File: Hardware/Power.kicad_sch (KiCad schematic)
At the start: 48 parts, among them U1 LT1963AEST-3.3#TRPBF, U2 TPS5405DR, U3 TPS2115ADRBR, U4 LT1963AEST-3.3#TRPBF

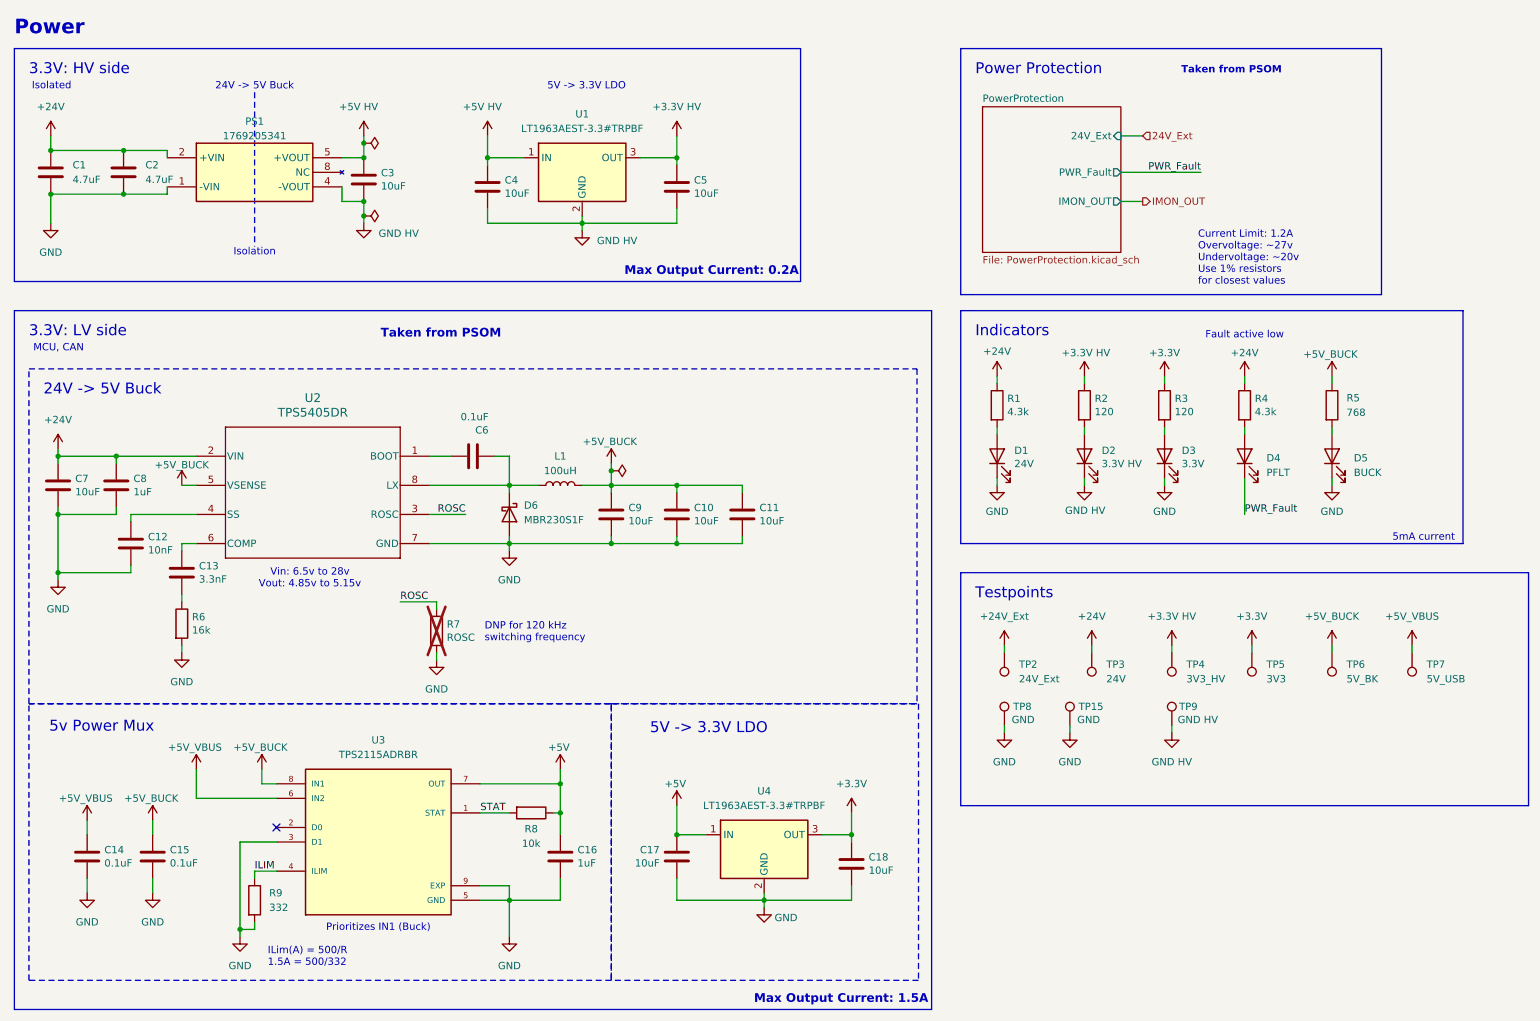
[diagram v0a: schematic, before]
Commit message: RevB Changes (#4)
* added documentation for current range; added VBUS led

* INA common-mode fixed (i think)

* differential amp for LPF

* diff amp / LPF

* some comments so I don't forget what I'm doing

* new TLV symbol, SPDT switch for scrut

* fixed LPF cutoff

* refactored and added LPF docs; added fuse, boot_gpio from USB-UART chip

* i lowk haven't started layout

* slightly cooked

* started layout not really but kind of

* layout stuff

* post review council sch changes: shielded connectors, removed SHDN resistor, diode OR for boot, standardized resistors

* starting routing i think

* almost done with routing

* wow

* drc is happy

* ye

* again

* addressed some comments

* added lcsc part numbers

* generated production files and docs

* updated STEP file

* symbol library

* addressed comments; generated production files, docs

* added Mouser BOM, deleted embedded step files
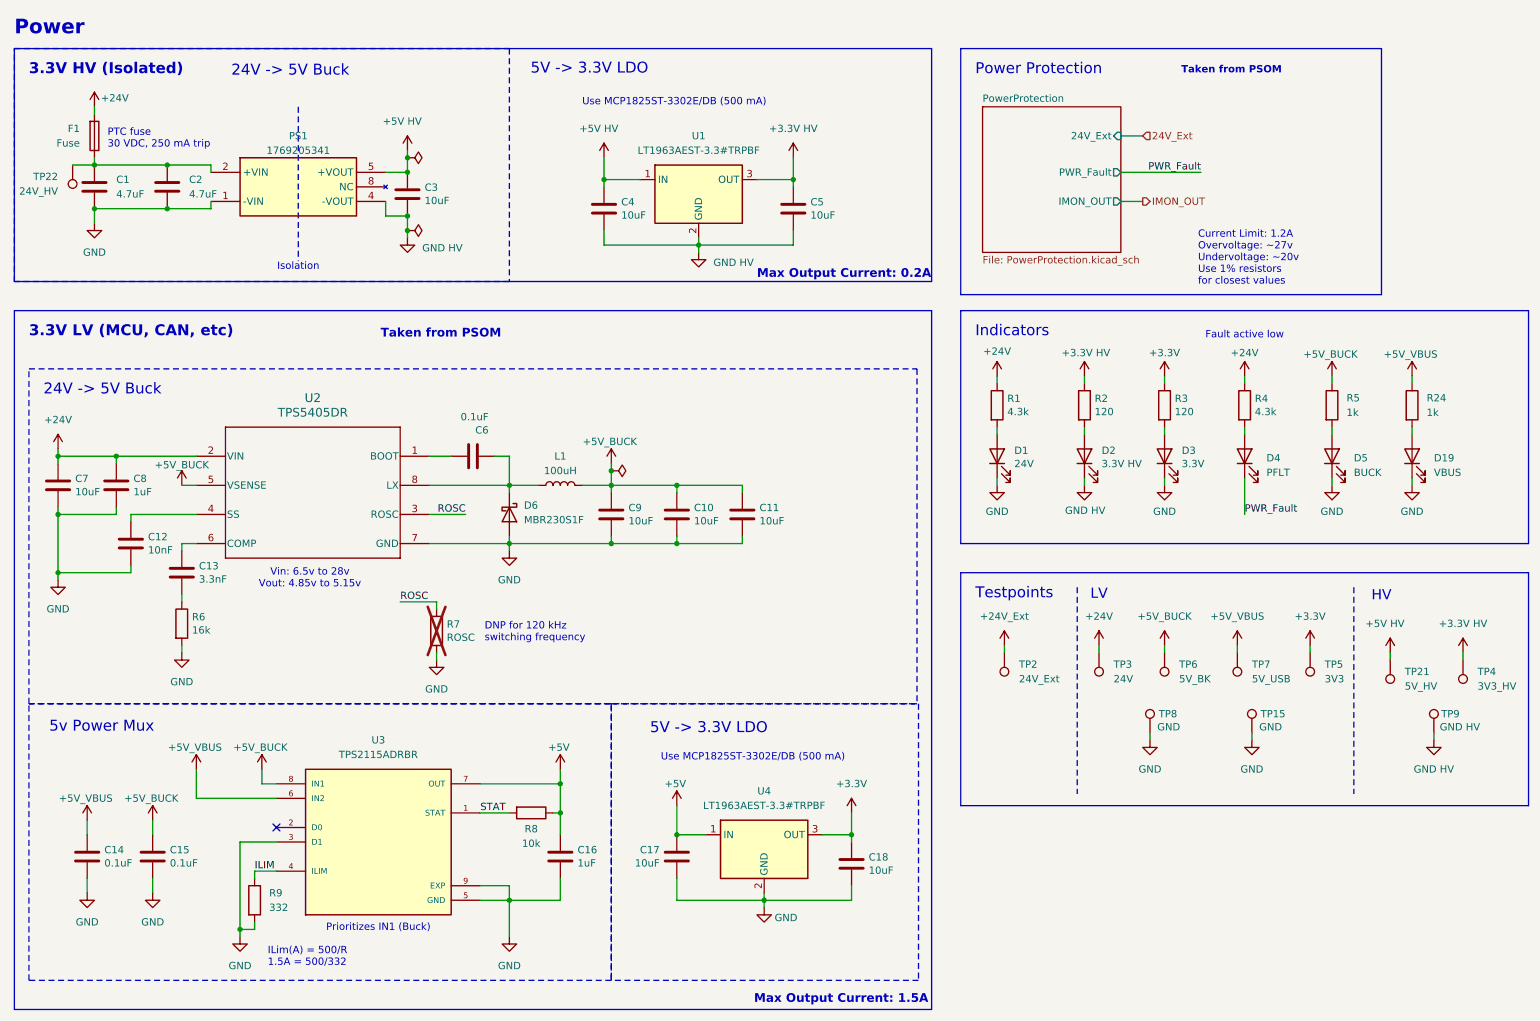
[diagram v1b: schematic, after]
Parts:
- added D19: VBUS, LED_SMD:LED_0603_1608Metric_Pad1.05x0.95mm_HandSolder, symbol Device:LED
- added F1: Fuse, Parts:FUSC3216X125N, symbol Device:Fuse
- added R24: 1k, Resistor_SMD:R_0603_1608Metric_Pad0.98x0.95mm_HandSolder, symbol Device:R
- added TP21: 5V_HV, TestPoint:TestPoint_Pad_1.0x1.0mm, symbol Connector:TestPoint
- added TP22: 24V_HV, TestPoint:TestPoint_Pad_1.0x1.0mm, symbol Connector:TestPoint
- R5: value 768 -> 1k
- TP15, TP8, TP9: footprint TestPoint:TestPoint_Pad_1.0x1.0mm -> Connector_PinHeader_2.54mm:PinHeader_1x01_P2.54mm_Vertical
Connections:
- net +24V: now also F1.2; no longer C1.1, C2.1, PS1.2 (+VIN)
- net +5V HV: now also TP21.1
- net +5V_VBUS: now also R24.1
- net GND: now also D19.1 (K)
- new net: C1.1, C2.1, F1.1, PS1.2 (+VIN), TP22.1
- new net: D19.2 (A), R24.2
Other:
- note added: "3.3V HV (Isolated)"
- note added: "3.3V LV (MCU, CAN, etc)"
- note added: "HV"
- note added: "LV"
- note added: "PTC fuse 30 VDC, 250 mA trip"
- note added: "Use MCP1825ST-3302E/DB (500 mA)"
- note removed: "3.3V: HV side"
- note removed: "3.3V: LV side"
- note removed: "5mA current"
- note removed: "Isolated"
- note removed: "MCU, CAN"
- moved on the sheet: C1, C2, C3, C4, C5, PS1, TP15, TP3, TP4, TP5, TP6, TP7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
